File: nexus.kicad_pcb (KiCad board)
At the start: 2 copper layers, 107 parts, among them J1 PIN6-9_Breakout, J10 Screw_Terminal_01x02, J11 24V_Lockout_Key_Switch, J12 XT60-M, J13 PT_1, J14 PT_4, J15 PT_2, J16 PT_5, J17 PT_3, J18 PT_6, J19 4-Pin Load Cell, J2 PIN10-13_Breakout, J20 5-Pin Load Cell, J21 Ignitor Screw Terminal, J3 Valve_1_PWR, J4 Valve_4_PWR, J5 Valve_2_PWR, J6 Valve_5_PWR, J7 Valve_3_PWR, J8 Valve_6_PWR, J9 Screw_Terminal_01x04, K1 G5LE-1, K2 G5LE-1, Q1 BSS138, Q2 BSS138, Q3 BSS138, Q4 BSS138, Q5 BSS138, Q6 BSS138, Q7 BSS138, Q8 BSS138, U1 ESP32-S3, U2 ADS112C04, U3 ADS112C04, U4 ADS112C04, U5 ADS112C04, U6 XC6206P332MR, U7 TPS5430DDA, U8 TPS5430DDA

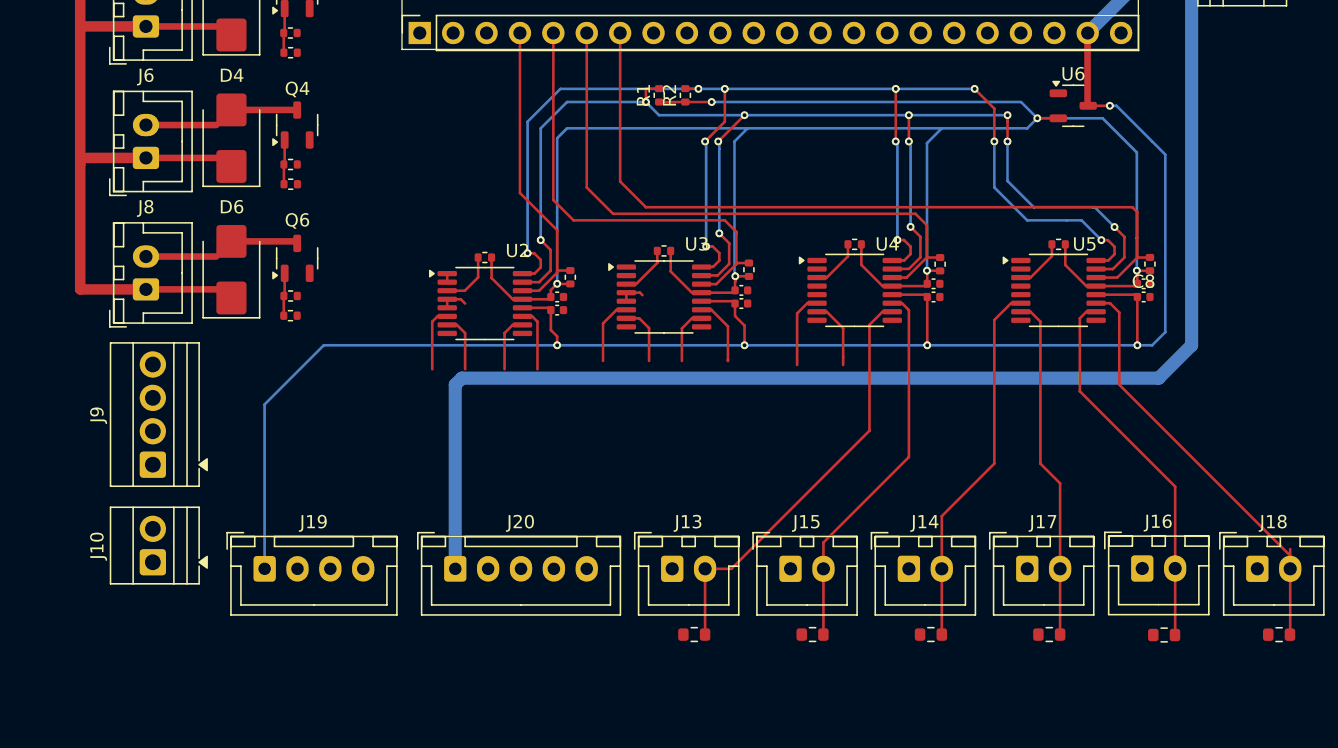
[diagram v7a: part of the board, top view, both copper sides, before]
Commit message: Route power to sensors
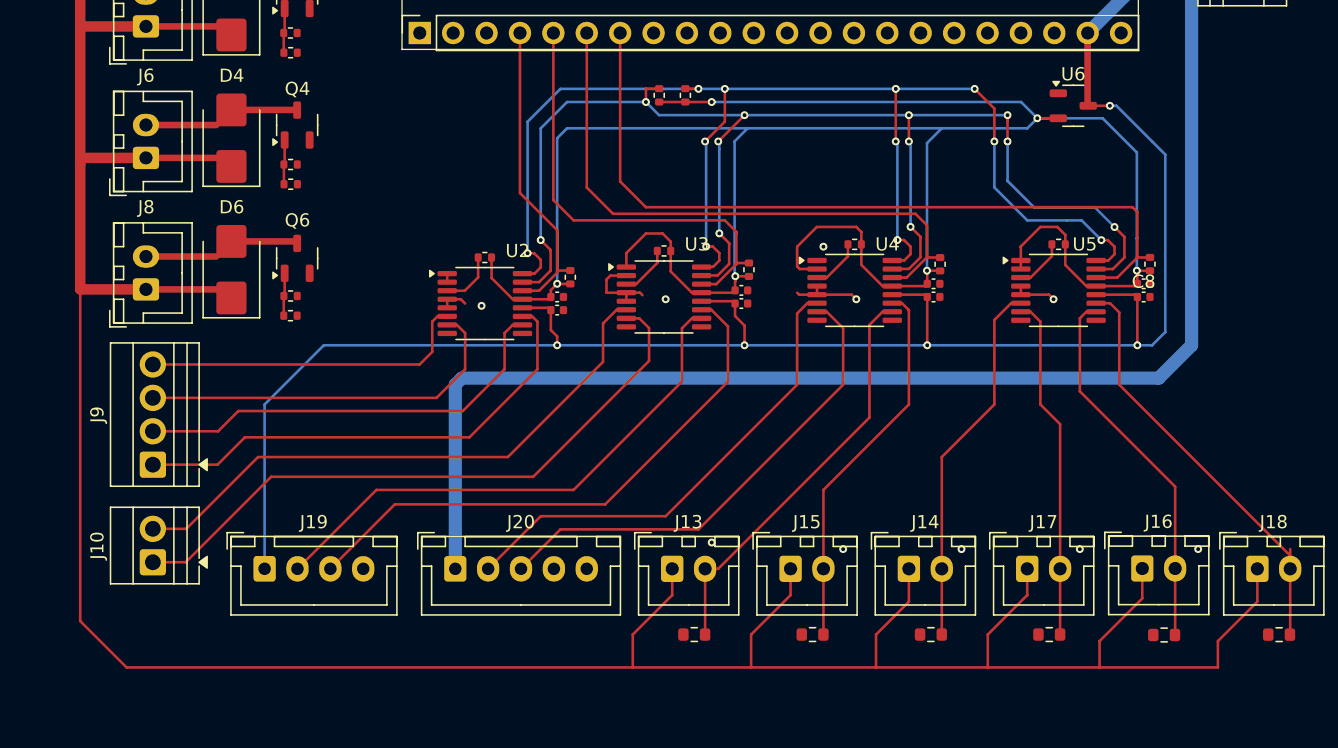
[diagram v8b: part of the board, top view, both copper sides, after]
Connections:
- U3 pad 10: LC_THRUST_+ -> LC_FILL_+
- U3 pad 11: LC_THRUST_- -> LC_FILL_-
- U4 pad 6: LC_FILL_+ -> LC_THRUST_+
- U4 pad 7: LC_FILL_- -> LC_THRUST_-
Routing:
- net +24V: track 254.6 -> 420.2 mm
- net /ADC Circuitry/ADC2_AIN2: track 4.53 -> 48.6 mm
- net /ADC Circuitry/ADC2_AIN3: track 5.06 -> 44.6 mm
- net LC_FILL_-: track 5.31 -> 42.9 mm
- net LC_FILL_+: track 5.76 -> 41.0 mm
- net LC_THRUST_+: track 4.29 -> 36.6 mm
- net /ADC Circuitry/ADC1_AIN0: track 4.93 -> 37.2 mm
- net LC_THRUST_-: track 5.26 -> 37.1 mm
- net /ADC Circuitry/ADC1_AIN1: track 4.37 -> 33.1 mm
- net /ADC Circuitry/ADC1_AIN2: track 4.37 -> 29.0 mm
- net +3.3V: track 157.2 -> 179.6 mm
- net /ADC Circuitry/ADC1_AIN3: track 4.93 -> 25.3 mm
- net GND: track 19.7 -> 32.5 mm, vias 0 -> 10
- net PT_READING_1: track 32.1 -> 31.5 mm
